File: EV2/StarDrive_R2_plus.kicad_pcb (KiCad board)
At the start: 4 copper layers, 195.6 x 49.5 mm, 49 parts, among them J1 Conn_02x06_Odd_Even, J2 Conn_02x06_Odd_Even, J3 Conn_02x17_Odd_Even, J4 Conn_02x13_Odd_Even, J5 DBG1, U1 PCF8573P, U2 74HCT74, U3 74HCT04, U4 AM5380, U5 SN74F32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

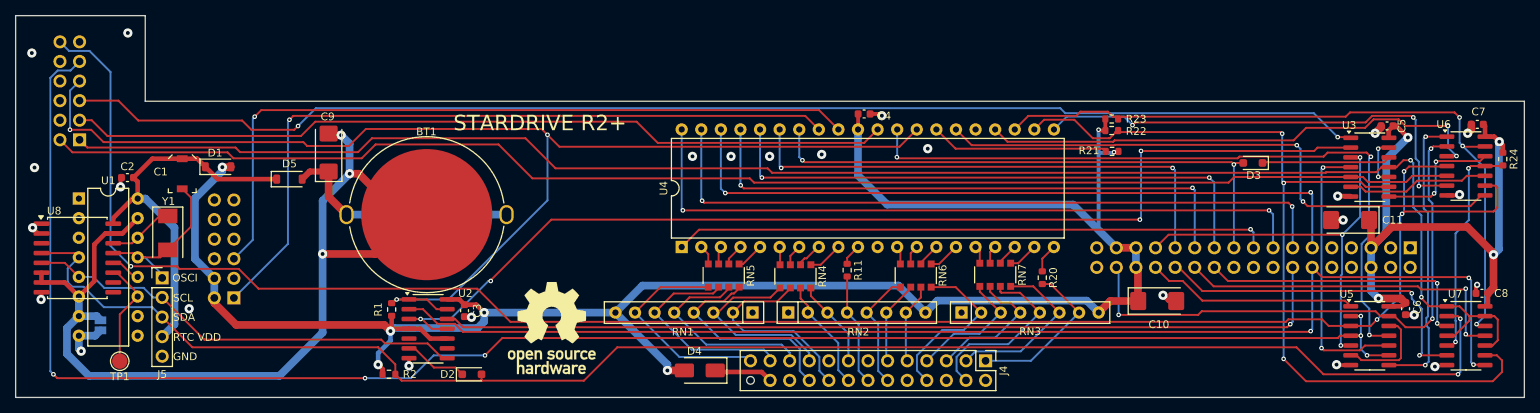
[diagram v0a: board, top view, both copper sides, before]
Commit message: Fix #3 #4
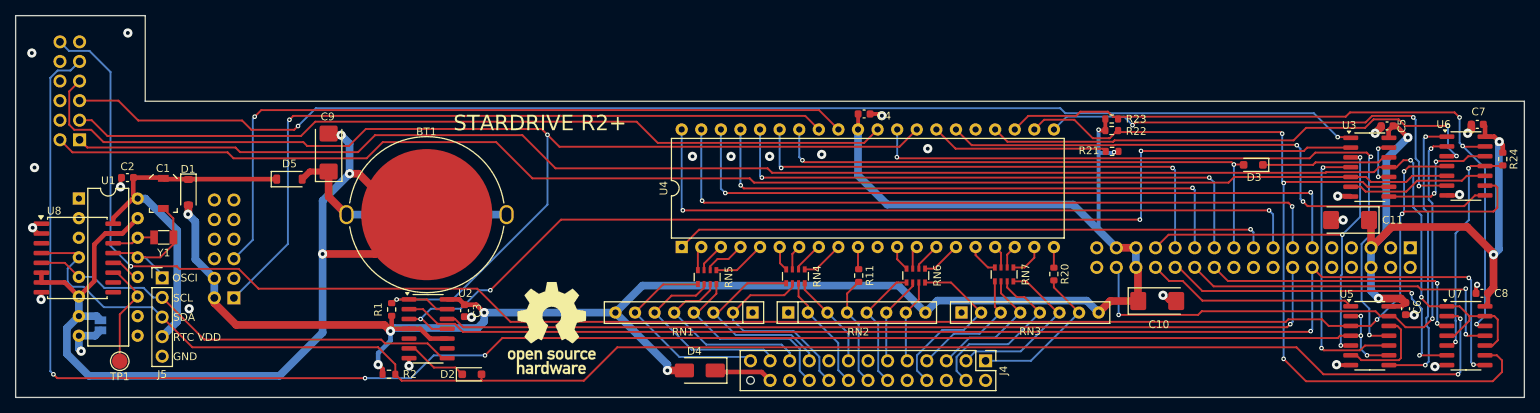
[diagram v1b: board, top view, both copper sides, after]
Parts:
- RN4, RN5, RN6, RN7: footprint Resistor_SMD:R_Array_Convex_4x1206 -> Resistor_SMD:R_Array_Convex_4x0603
- Y1: footprint Crystal:Crystal_SMD_0603-2Pin_6.0x3.5mm -> Crystal:Crystal_SMD_3215-2Pin_3.2x1.5mm
- moved D1 5.07 mm to (72.4, 72.9), turned to -90 degrees
- moved C1 3.54 mm to (69.2, 73.0)
- moved RN5 2.16 mm to (139.7, 83.9)
- moved R11 1.66 mm to (159.3, 83.7)
- moved R20 1.57 mm to (184.6, 83.5)
- moved RN7 1.15 mm to (178.2, 83.5)
- moved Y1 0.78 mm to (69.2, 78.8), turned to 180 degrees
- moved D3 0.25 mm to (210.4, 69.3)
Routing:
- net VCC: track 342.3 -> 335.2 mm
- net /OSCI: track 21.5 -> 18.0 mm
- net /DB4: track 3.62 -> 6.90 mm
- net /DB5: track 2.83 -> 5.46 mm
- net /DB6: track 1.91 -> 3.92 mm
- net /_DB4: track 27.5 -> 25.5 mm
- net /RST: track 2.33 -> 4.21 mm
- net /OSCO: track 7.47 -> 5.62 mm
- net /RTC_VDD: track 49.7 -> 48.0 mm
- net /_DB5: track 26.5 -> 24.8 mm
- net /SEL: track 1.79 -> 3.30 mm
- net /_DB6: track 26.9 -> 25.5 mm
- net /_DB7: track 27.7 -> 26.5 mm
- net /REQ: track 3.78 -> 2.68 mm
- net /_SEL: track 15.7 -> 16.7 mm
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
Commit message: Remove SMD resistor arrays with individual resistors and switch to hand-solder footprints.
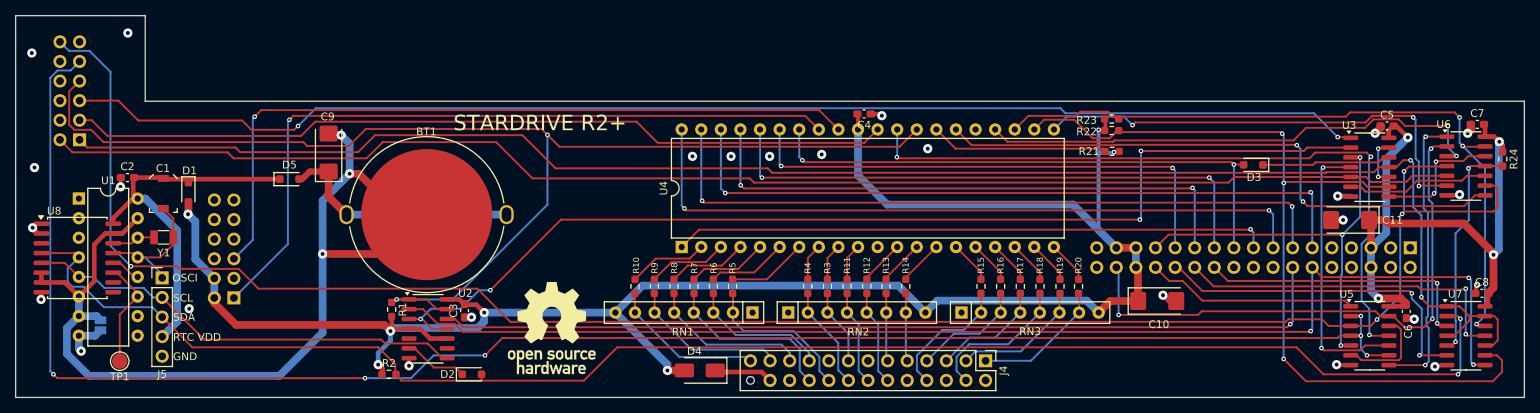
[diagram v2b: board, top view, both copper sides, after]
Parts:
- removed RN4, RN5, RN6, RN7: CAY16-10R0F4LF, Resistor_SMD:R_Array_Convex_4x0603
- added R10: 10, Resistor_SMD:R_0603_1608Metric_Pad0.98x0.95mm_HandSolder, F.Cu at (130.3, 85.1)
- added R12: 10, Resistor_SMD:R_0603_1608Metric_Pad0.98x0.95mm_HandSolder, F.Cu at (160.3, 85.1)
- added R13: 10, Resistor_SMD:R_0603_1608Metric_Pad0.98x0.95mm_HandSolder, F.Cu at (162.8, 85.1)
- added R14: 10, Resistor_SMD:R_0603_1608Metric_Pad0.98x0.95mm_HandSolder, F.Cu at (165.4, 85.1)
- added R15: 10, Resistor_SMD:R_0603_1608Metric_Pad0.98x0.95mm_HandSolder, F.Cu at (175.2, 85.1)
- added R16: 10, Resistor_SMD:R_0603_1608Metric_Pad0.98x0.95mm_HandSolder, F.Cu at (177.7, 85.1)
- added R17: 10, Resistor_SMD:R_0603_1608Metric_Pad0.98x0.95mm_HandSolder, F.Cu at (180.2, 85.1)
- added R18: 10, Resistor_SMD:R_0603_1608Metric_Pad0.98x0.95mm_HandSolder, F.Cu at (182.8, 85.1)
- added R19: 10, Resistor_SMD:R_0603_1608Metric_Pad0.98x0.95mm_HandSolder, F.Cu at (185.4, 85.1)
- added R3: 10, Resistor_SMD:R_0603_1608Metric_Pad0.98x0.95mm_HandSolder, F.Cu at (155.2, 85.1)
- added R4: 10, Resistor_SMD:R_0603_1608Metric_Pad0.98x0.95mm_HandSolder, F.Cu at (152.7, 85.1)
- added R5: 10, Resistor_SMD:R_0603_1608Metric_Pad0.98x0.95mm_HandSolder, F.Cu at (142.9, 85.1)
- added R6: 10, Resistor_SMD:R_0603_1608Metric_Pad0.98x0.95mm_HandSolder, F.Cu at (140.4, 85.1)
- added R7: 10, Resistor_SMD:R_0603_1608Metric_Pad0.98x0.95mm_HandSolder, F.Cu at (137.9, 85.1)
- added R8: 10, Resistor_SMD:R_0603_1608Metric_Pad0.98x0.95mm_HandSolder, F.Cu at (135.3, 85.1)
- added R9: 10, Resistor_SMD:R_0603_1608Metric_Pad0.98x0.95mm_HandSolder, F.Cu at (132.8, 85.1)
- C2, C3, C4, C5, C6, C7, C8: footprint Capacitor_SMD:C_0603_1608Metric -> Capacitor_SMD:C_0603_1608Metric_Pad1.08x0.95mm_HandSolder
- D1, D5: footprint Diode_SMD:D_SOD-123 -> Diode_SMD:D_SOD-323_HandSoldering
- R1, R11, R2, R20, R21, R22, R23, R24: footprint Resistor_SMD:R_0603_1608Metric -> Resistor_SMD:R_0603_1608Metric_Pad0.98x0.95mm_HandSolder
- moved R20 3.58 mm to (187.8, 85.1)
- moved R11 2.05 mm to (157.8, 85.1)
- moved C6 0.36 mm to (230.3, 88.3)
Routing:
- net /_DB3: track 26.0 -> 18.1 mm
- net /_DB7: track 26.5 -> 19.3 mm
- net /DB3: track 3.18 -> 10.3 mm
- net /DB7: track 3.18 -> 10.3 mm
- net /DB2: track 3.27 -> 10.4 mm
- net /_DB2: track 27.3 -> 20.4 mm
- net /DB6: track 3.92 -> 10.4 mm
- net /_ATN: track 23.3 -> 16.9 mm
- net /_DB6: track 25.5 -> 20.1 mm
- net /_MSG: track 22.4 -> 17.2 mm
- net /DB5: track 5.46 -> 10.4 mm
- net /_SEL: track 16.7 -> 12.4 mm
- net /_DB5: track 24.8 -> 20.8 mm
- net /_C_D: track 23.1 -> 19.2 mm
- net /DB4: track 6.90 -> 10.3 mm
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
